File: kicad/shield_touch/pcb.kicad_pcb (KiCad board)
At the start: 2 copper layers, 48.9 x 49.5 mm, 0 parts

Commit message: update
- still to fix
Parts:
- added C1: 0.01uF, Capacitors_THT:C_Disc_D5.0mm_W2.5mm_P2.50mm, F.Cu at (92.6, 99.1)
- added C2: 0.01uF, Capacitors_THT:C_Disc_D5.0mm_W2.5mm_P2.50mm, F.Cu at (92.7, 104.6)
- added C3: 0.01uF, Capacitors_THT:C_Disc_D5.0mm_W2.5mm_P2.50mm, F.Cu at (99.4, 104.5)
- added J1: Conn_01x12_Fem_l, Connectors_Samtec:SL-112-X-XX_1x12, F.Cu at (104.3, 67.1)
- added J2: Conn_01x12_Fem_r, Connectors_Samtec:SL-112-X-XX_1x12, F.Cu at (119.5, 67.1)
- added J3: Conn_01x09_Fem_b_l, Connectors_Samtec:SL-110-X-XX_1x10, F.Cu at (92.8, 68.6)
- added J4: Conn_01x11_Fem_b_r_touch, Connectors_Samtec:SL-111-X-XX_1x11, F.Cu at (134.0, 71.8)
- added R1: 2M, Resistors_THT:R_Axial_DIN0207_L6.3mm_D2.5mm_P10.16mm_Horizontal, F.Cu at (108.3, 65.0)
- added R10: 2M, Resistors_THT:R_Axial_DIN0207_L6.3mm_D2.5mm_P10.16mm_Horizontal, F.Cu at (112.0, 101.2)
- added R11: 2M, Resistors_THT:R_Axial_DIN0207_L6.3mm_D2.5mm_P10.16mm_Horizontal, F.Cu at (108.3, 101.2)
- added R12: 2M, Resistors_THT:R_Axial_DIN0207_L6.3mm_D2.5mm_P10.16mm_Horizontal, F.Cu at (115.7, 88.1)
- added R13: 2M, Resistors_THT:R_Axial_DIN0207_L6.3mm_D2.5mm_P10.16mm_Horizontal, F.Cu at (112.0, 88.1)
- added R14: 2M, Resistors_THT:R_Axial_DIN0207_L6.3mm_D2.5mm_P10.16mm_Horizontal, F.Cu at (100.6, 64.3)
- added R15: 2M, Resistors_THT:R_Axial_DIN0207_L6.3mm_D2.5mm_P10.16mm_Horizontal, F.Cu at (128.1, 86.4)
- added R2: 2M, Resistors_THT:R_Axial_DIN0207_L6.3mm_D2.5mm_P10.16mm_Horizontal, F.Cu at (112.0, 65.0)
- added R3: 2M, Resistors_THT:R_Axial_DIN0207_L6.3mm_D2.5mm_P10.16mm_Horizontal, F.Cu at (115.7, 65.0)
- added R4: 2M, Resistors_THT:R_Axial_DIN0207_L6.3mm_D2.5mm_P10.16mm_Horizontal, F.Cu at (108.3, 88.1)
- added R5: 2M, Resistors_THT:R_Axial_DIN0207_L6.3mm_D2.5mm_P10.16mm_Horizontal, F.Cu at (100.6, 100.2)
- added R6: 2M, Resistors_THT:R_Axial_DIN0207_L6.3mm_D2.5mm_P10.16mm_Horizontal, F.Cu at (124.3, 88.6)
- added R7: 2M, Resistors_THT:R_Axial_DIN0207_L6.3mm_D2.5mm_P10.16mm_Horizontal, F.Cu at (124.3, 102.1)
- added R8: 2M, Resistors_THT:R_Axial_DIN0207_L6.3mm_D2.5mm_P10.16mm_Horizontal, F.Cu at (124.3, 64.1)
- added R9: 2M, Resistors_THT:R_Axial_DIN0207_L6.3mm_D2.5mm_P10.16mm_Horizontal, F.Cu at (115.7, 101.2)
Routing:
- net VCC: track 0.00 -> 70.3 mm
- net GND: track 0.00 -> 20.8 mm
- net 16: track 0.00 -> 14.4 mm
- net 14: track 0.00 -> 13.7 mm
- net A0: track 0.00 -> 13.1 mm
- net 21: track 0.00 -> 13.1 mm
- net 10: track 0.00 -> 13.1 mm
- net 15: track 0.00 -> 13.1 mm
- net A2: track 0.00 -> 13.1 mm
- net A1: track 0.00 -> 13.1 mm
- added copper zone on B.Cu, net GND
- added copper zone on F.Cu, net GND
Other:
- board text added: "21"
- board text added: "USB"
- board text added: "VCC"
- board text removed: "12"
- board text removed: "Arduino Pro Micro Leonardo"
- board text removed: "Insert here your"
- board text removed: "Play your simulation games with"
- board text removed: "USB HID device Plug and Play Small and Cute :)"
- board text removed: "Volante"

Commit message: update
- still to fix
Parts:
- moved R10 38.6 mm to (123.1, 64.3), turned to 0 degrees
- moved R11 38.0 mm to (113.0, 63.5), turned to 180 degrees
- moved R15 27.6 mm to (100.6, 87.5)
- moved R9 24.6 mm to (124.1, 78.1)
- moved R4 20.8 mm to (128.1, 94.5)
- moved R1 18.2 mm to (115.8, 81.7)
- moved R3 18.0 mm to (108.8, 81.7)
- moved R6 17.4 mm to (128.1, 71.6), turned to 270 degrees
- moved R2 16.6 mm to (112.3, 81.7)
- moved R12 9.65 mm to (112.3, 79.1)
- moved R13 9.56 mm to (108.8, 79.1)
- moved R8 8.42 mm to (116.0, 63.4)
- moved R7 1.30 mm to (124.6, 100.8)
- moved R14 0.64 mm to (99.9, 64.3)
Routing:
- net VCC: track 70.3 -> 0.00 mm
- net GND: track 20.8 -> 0.00 mm
- net 16: track 14.4 -> 0.00 mm
- net 14: track 13.7 -> 0.00 mm
- net A0: track 13.1 -> 0.00 mm
- net 21: track 13.1 -> 0.00 mm
- net 10: track 13.1 -> 0.00 mm
- net A2: track 13.1 -> 0.13 mm
- net A1: track 13.1 -> 0.25 mm
- net 15: track 13.1 -> 0.38 mm
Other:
- board text added: "Touch Technology"

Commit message: update
- still working
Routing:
- net VCC: track 0.00 -> 163.8 mm
- net 4: track 0.00 -> 64.1 mm
- net 6: track 0.00 -> 56.7 mm
- net 1: track 0.00 -> 37.4 mm, vias 0 -> 1
- net A1: track 0.25 -> 36.3 mm, vias 0 -> 1
- net A2: track 0.13 -> 35.1 mm, vias 0 -> 1
- net A0: track 0.00 -> 33.1 mm, vias 0 -> 1
- net 2: track 0.00 -> 32.1 mm
- net 21: track 0.00 -> 24.9 mm
- net 14: track 0.00 -> 24.4 mm, vias 0 -> 1
- net 15: track 0.38 -> 24.1 mm, vias 0 -> 1
- net 9: track 0.00 -> 22.7 mm
- net 0: track 0.00 -> 21.7 mm
- net 7: track 0.00 -> 20.6 mm
- net 8: track 0.00 -> 19.6 mm
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
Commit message: update
- still working
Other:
- board text added: "- I/O are pull-high - use resistors >= 2.2M - connect to ground using 100KOhm objects (your finger) - Enjoy!!!"
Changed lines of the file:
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@@
     (area 88.799999 60.859999 137.895001 110.590001)
     (thickness 1.6)
-    (drawings 77)
+    (drawings 78)
     (tracks 194)
     (zones 0)
@@
   (page A4)
   (layers
-    (0 F.Cu signal)
-    (31 B.Cu signal)
+    (0 F.Cu signal hide)
+    (31 B.Cu signal hide)
     (32 B.Adhes user)
     (33 F.Adhes user)
@@
     )
   )
+  (gr_text "- I/O are pull-high\n- use resistors >= 2.2M\n- connect to ground using \n   100KOhm objects (your finger)\n- Enjoy!!!" (at 116.078 105.156) (layer B.SilkS)
+    (effects (font (size 1 1) (thickness 0.1)) (justify mirror))
+  )
   (gr_line (start 112.0775 106.2355) (end 111.633 105.791) (angle 90) (layer F.SilkS) (width 0.2))
   (gr_line (start 112.8395 105.4735) (end 112.0775 106.2355) (angle 90) (layer F.SilkS) (width 0.2))
@@
     (effects (font (size 1.2 1.2) (thickness 0.1)))
   )
-  (gr_text "By Andrea Mancini" (at 124.714 107.442) (layer F.SilkS)
-    (effects (font (size 1.2 1.2) (thickness 0.1)))
-  )
-  (gr_text "            Volante \nThe Gamepad" (at 126.111 103.886) (layer F.SilkS)
-    (effects (font (size 1.5 1.5) (thickness 0.3)))
+  (gr_text "By Andrea Mancini" (at 128.016 107.442) (layer F.SilkS)
+    (effects (font (size 1.2 1.2) (thickness 0.1)))
+  )
+  (gr_text "           Volante \nThe Gamepad" (at 136.398 103.632) (layer F.SilkS)
+    (effects (font (size 1.5 1.5) (thickness 0.3)) (justify right))
   )
   (gr_line (start 137.795 110.49) (end 88.9 110.49) (angle 90) (layer Edge.Cuts) (width 0.2))

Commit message: update
- still to fix
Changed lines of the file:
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@@
   (page A4)
   (layers
-    (0 F.Cu signal hide)
-    (31 B.Cu signal hide)
+    (0 F.Cu signal)
+    (31 B.Cu signal)
     (32 B.Adhes user)
     (33 F.Adhes user)
     (34 B.Paste user)
     (35 F.Paste user)
-    (36 B.SilkS user hide)
+    (36 B.SilkS user)
     (37 F.SilkS user)
     (38 B.Mask user)
@@
     (descr "Low profile, screw machine socket strip, through hole, 100mil / 2.54mm pitch")
     (tags "samtec socket strip tht single")
-    (fp_text reference J1 (at -2.27 13.97 90) (layer F.SilkS)
-      (effects (font (size 1 1) (thickness 0.15)))
-    )
+    (fp_text reference J1 (at 0.127 31.242 90) (layer F.SilkS)
+      (effects (font (size 1 1) (thickness 0.15)))
+    )

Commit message: update
- almost finished
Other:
- board text added: "Arduino Pro Micro Leonardo"
- board text added: "GAMEPAD BOX"
- board text added: "PC"

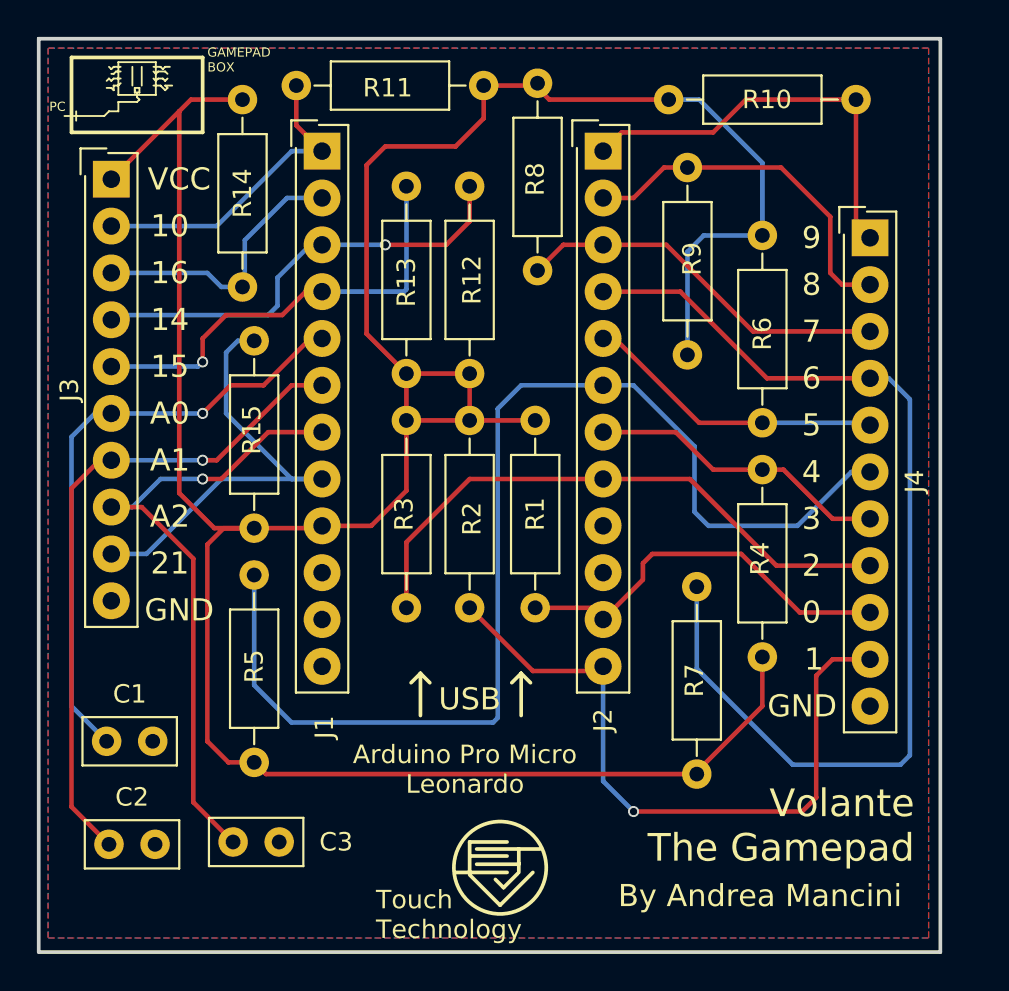
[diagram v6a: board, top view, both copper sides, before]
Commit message: update
- designing pcb with vertical resistors
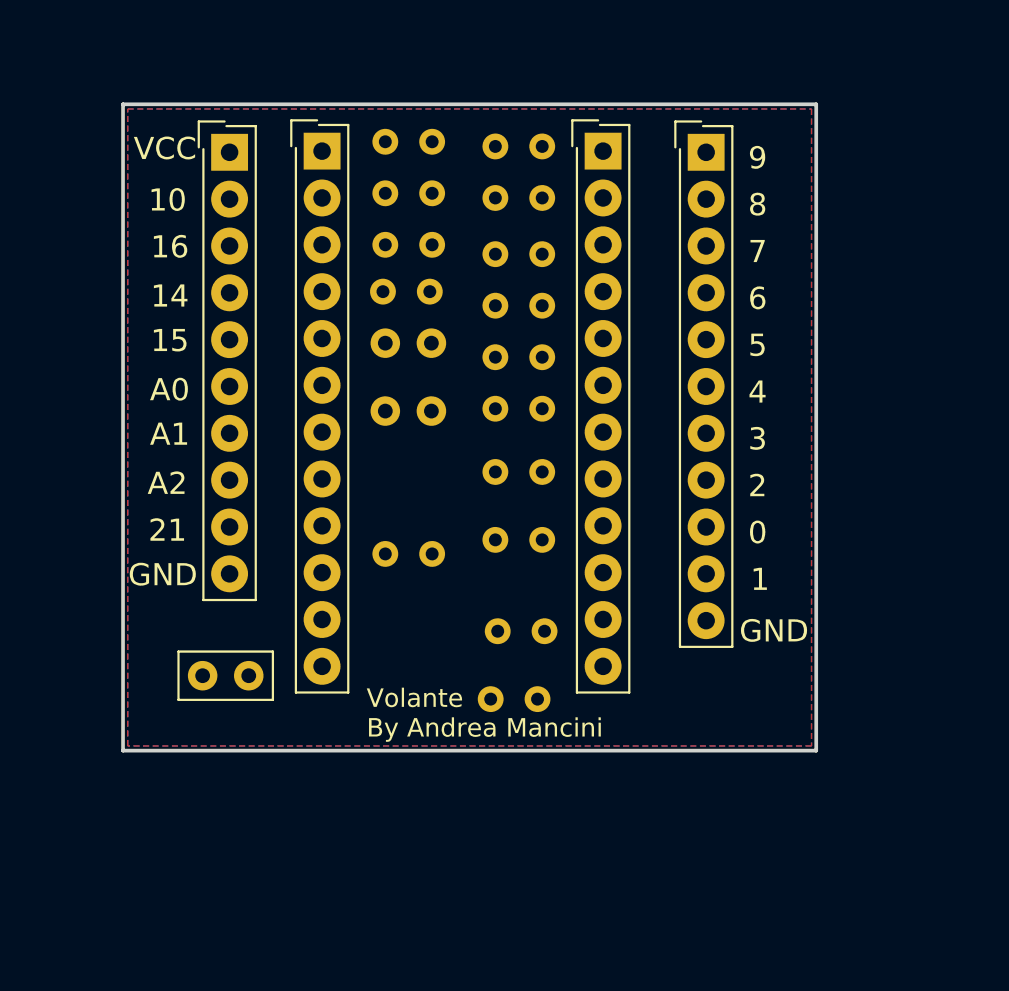
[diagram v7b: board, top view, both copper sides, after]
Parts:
- C1, C2: moved to B.Cu
- R1, R10, R11, R12, R13, R14, R15, R2, R3, R4, R5, R6, R7, R8, R9: footprint Resistors_THT:R_Axial_DIN0207_L6.3mm_D2.5mm_P10.16mm_Horizontal -> Resistors_THT:R_Axial_DIN0204_L3.6mm_D1.6mm_P2.54mm_Vertical; moved to B.Cu
- moved C2 27.9 mm to (107.7, 81.2)
- moved R7 27.6 mm to (113.7, 75.4), turned to 0 degrees
- moved C1 26.4 mm to (107.7, 77.5)
- moved R5 23.2 mm to (113.7, 81.0), turned to 0 degrees
- moved R4 17.6 mm to (113.7, 84.5), turned to 0 degrees
- moved R6 15.9 mm to (113.7, 78.2), turned to 0 degrees
- moved R2 15.2 mm to (113.4, 96.8), turned to 0 degrees
- moved R9 13.4 mm to (113.7, 69.6), turned to 0 degrees
- moved R1 11.6 mm to (113.8, 93.1), turned to 0 degrees
- moved J4 10.0 mm to (125.1, 67.1)
- moved R10 9.74 mm to (113.7, 66.8)
- moved R8 9.55 mm to (113.7, 72.6), turned to 0 degrees
- moved R14 9.26 mm to (107.7, 69.3), turned to 0 degrees
- moved C3 9.17 mm to (97.8, 95.5)
- moved R12 8.35 mm to (107.7, 72.1), turned to 0 degrees
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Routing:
- net VCC: track 163.8 -> 0.00 mm
- net 4: track 64.1 -> 0.00 mm
- net 6: track 56.7 -> 0.00 mm
- net 1: track 37.4 -> 0.00 mm, vias 1 -> 0
- net A1: track 36.3 -> 0.00 mm, vias 1 -> 0
- net A2: track 35.1 -> 0.00 mm, vias 1 -> 0
- net A0: track 33.1 -> 0.00 mm, vias 1 -> 0
- net 2: track 32.1 -> 0.00 mm
- net 21: track 24.9 -> 0.00 mm
- net 14: track 24.4 -> 0.00 mm, vias 1 -> 0
- net 15: track 24.1 -> 0.00 mm, vias 1 -> 0
- net 9: track 22.7 -> 0.00 mm
- net 0: track 21.7 -> 0.00 mm
- net 7: track 20.6 -> 0.00 mm
- net 8: track 19.6 -> 0.00 mm
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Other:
- board size 48.9 x 49.5 mm -> 37.6 x 35.1 mm
- board text added: "Volante By Andrea Mancini"
- board text removed: "- I/O are pull-high - use resistors >= 2.2M - connect to ground using 100KOhm objects (your finger) - Enjoy!!!"
- board text removed: "Arduino Pro Micro Leonardo"
- board text removed: "By Andrea Mancini"
- board text removed: "GAMEPAD BOX"
- board text removed: "PC"
- board text removed: "Touch Technology"
- board text removed: "USB"
- board text removed: "Volante The Gamepad"

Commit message: update
- pcb complete and tested
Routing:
- net VCC: track 0.00 -> 69.1 mm
- net GND: track 0.00 -> 54.8 mm, vias 0 -> 1
- net A2: track 0.00 -> 20.0 mm
- net 21: track 0.00 -> 14.1 mm
- net 14: track 0.00 -> 13.1 mm
- net 16: track 0.00 -> 13.1 mm
- net 1: track 0.00 -> 12.0 mm
- net 0: track 0.00 -> 11.1 mm
- net 2: track 0.00 -> 10.8 mm
- net 10: track 0.00 -> 10.2 mm
- net A1: track 0.00 -> 10.1 mm
- net 3: track 0.00 -> 9.76 mm
- net A0: track 0.00 -> 9.63 mm
- net 15: track 0.00 -> 9.40 mm
- net 4: track 0.00 -> 9.39 mm
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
